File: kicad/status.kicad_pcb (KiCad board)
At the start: 4 copper layers, 84.1 x 61.7 mm, 49 parts, among them J1 Bus_PCI_Express_x1, J2 PPTC041LGBN-RC, J3 Conn_01x04, J4 503398-1892, J6 USB_C_Receptacle_USB2.0_16P, J7 Conn_01x02, U1 MCP25625T-E/ML, U2 RP2040, U4 W25Q128JVP, X1 ABM8-272-T3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

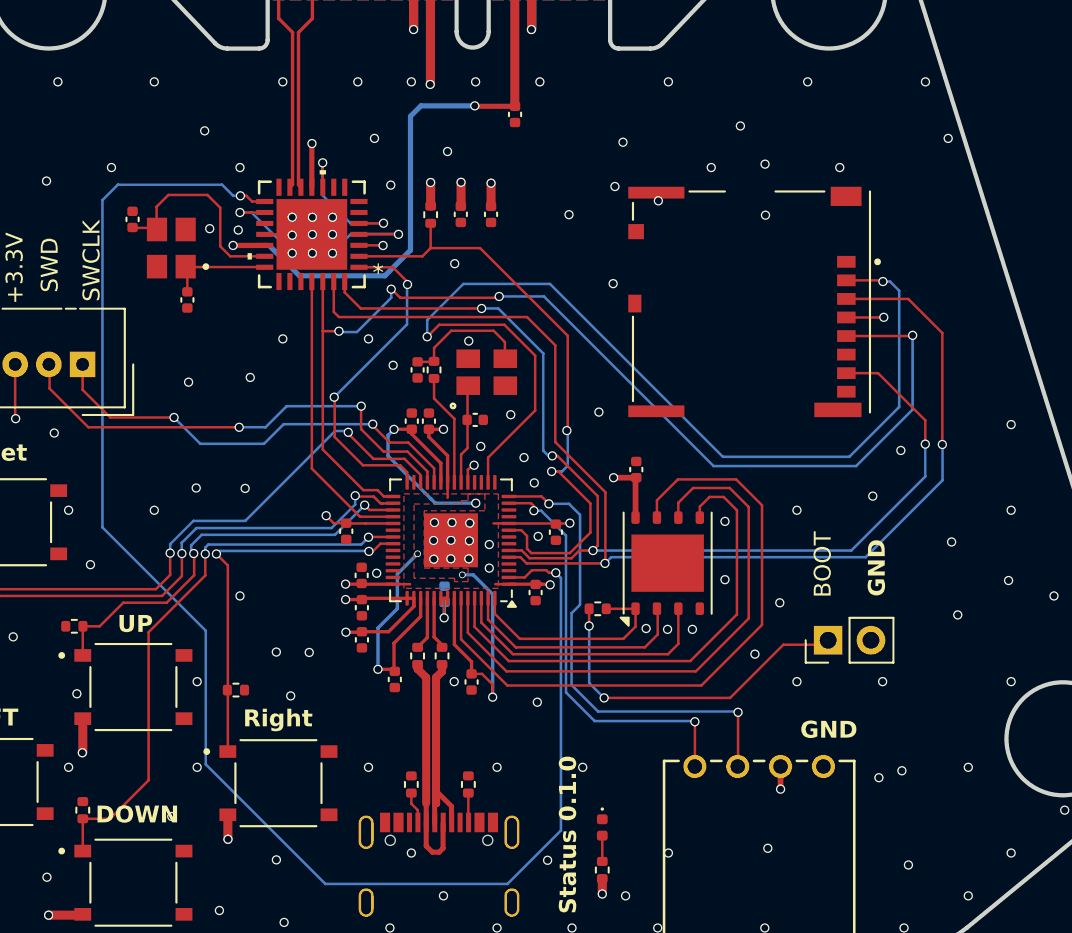
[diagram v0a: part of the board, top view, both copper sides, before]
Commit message: Pcb layout updated
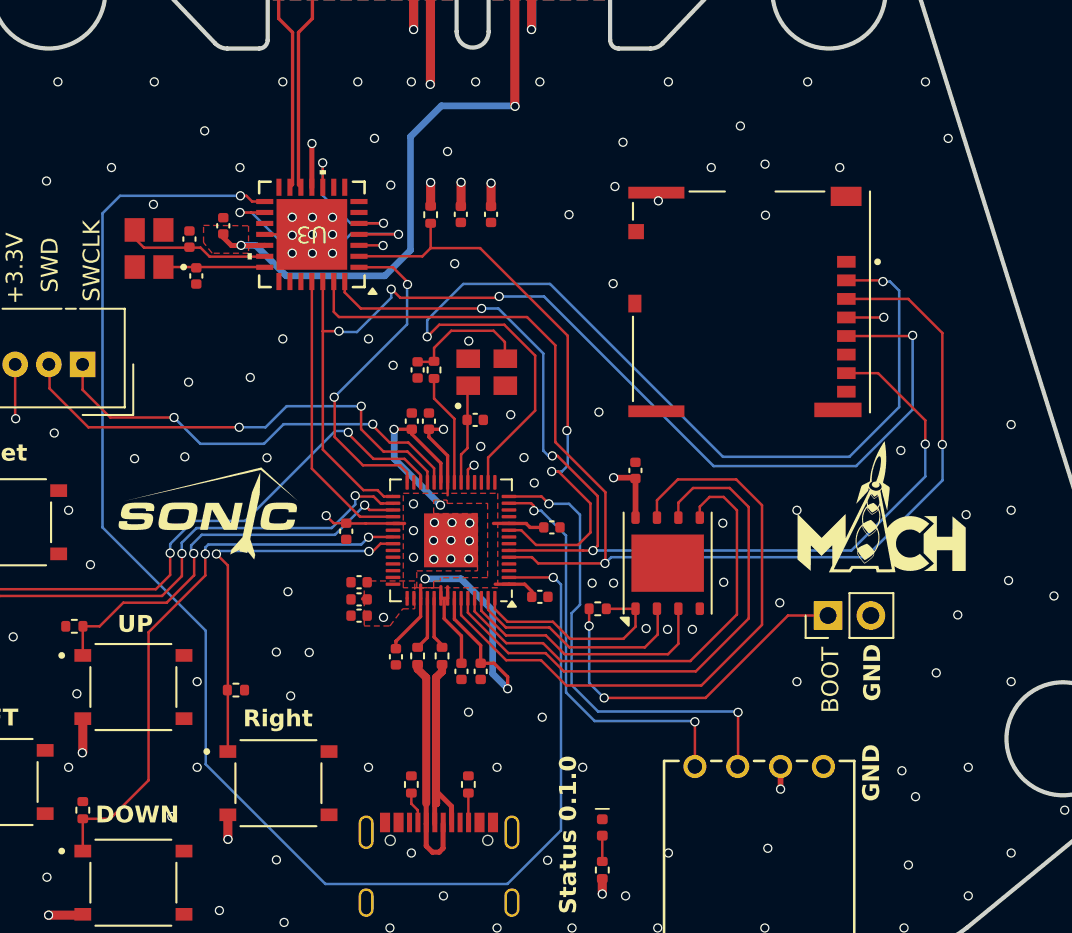
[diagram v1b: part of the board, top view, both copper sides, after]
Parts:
- removed U1: MCP25625T-E/ML, challenge_template:QFN28_6X6MC_MCH
- added G***: LOGO, LOGO, F.Cu at (172.7, 97.3)
- added U3: MCP25625T-E/ML, challenge_template:QFN28_6X6MC_MCH, F.Cu at (138.9, 80.2)
- C11: moved to F.Cu
- moved C3 18.5 mm to (133.6, 79.7), turned to -90 degrees
- moved C11 4.68 mm to (147.8, 106.1), turned to 90 degrees
- moved C6 3.57 mm to (131.6, 80.4)
- moved C22 1.52 mm to (132.0, 82.6)
- moved J7 1.47 mm to (169.5, 102.8)
- moved C13 1.44 mm to (141.7, 102.8), turned to 0 degrees
- moved C9 1.34 mm to (143.9, 105.2)
- moved Y1 1.32 mm to (129.2, 81.0)
- moved C8 0.83 mm to (148.9, 106.1)
- moved C12 0.52 mm to (141.7, 101.8), turned to 0 degrees
- moved C14 0.43 mm to (141.7, 100.8), turned to 0 degrees
- moved C15 0.37 mm to (153.1, 97.5), turned to 180 degrees
- moved C7 0.36 mm to (152.4, 101.7), turned to 180 degrees
- moved C17 0.07 mm to (158.1, 94.2)
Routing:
- net +3.3V: track 81.5 -> 70.6 mm, vias 27 -> 23
- net +1V1: track 42.6 -> 32.1 mm, vias 6 -> 4
- net /OSC2: track 12.2 -> 8.66 mm
- net /STBY: track 90.3 -> 88.7 mm
- net +5V: track 48.5 -> 49.7 mm
- net /RESET: track 36.2 -> 35.4 mm
- net /QSPI_SD3: track 38.4 -> 37.6 mm
- net /QSPI_CLK: track 33.4 -> 32.7 mm
- net /~{USB_BOOT_S}: track 20.3 -> 21.0 mm
- net /QSPI_SD0: track 28.8 -> 28.3 mm
- net GND: track 4.24 -> 4.44 mm, vias 144 -> 141
- added copper zone on F.Cu, net +5V

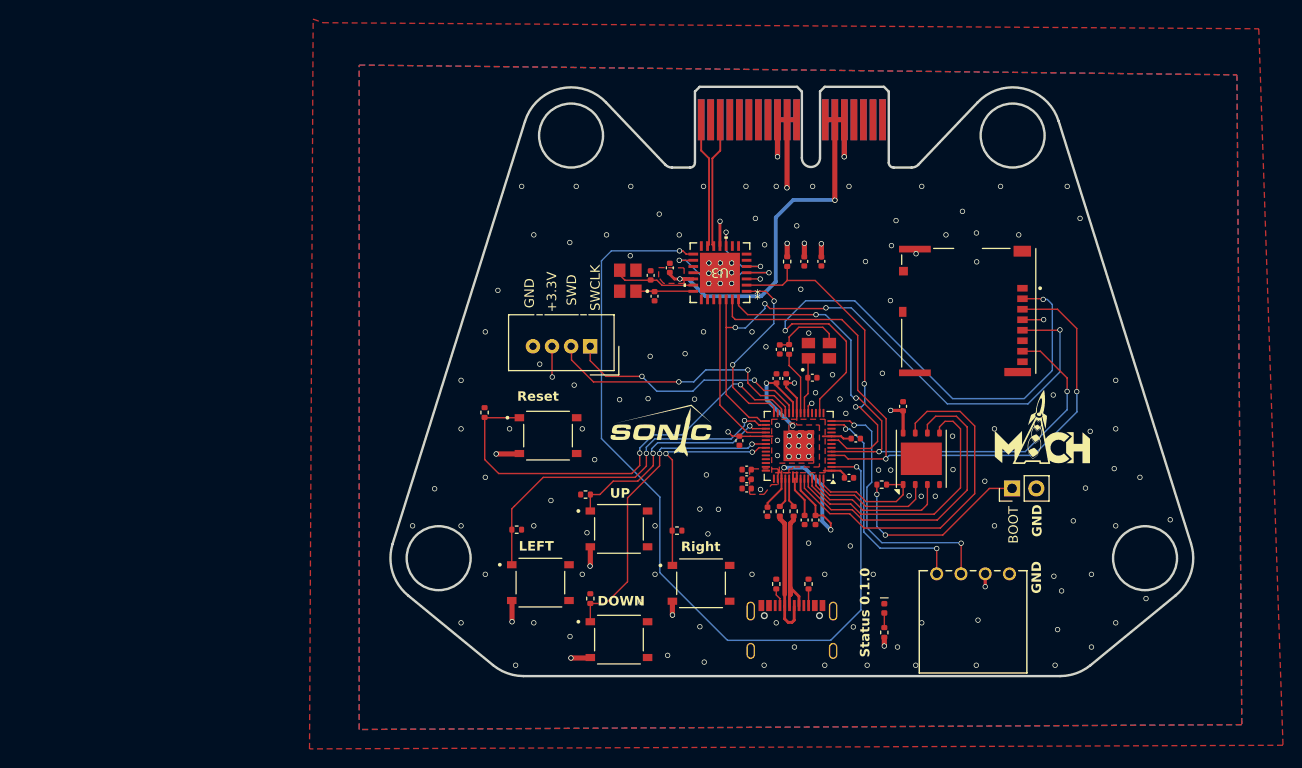
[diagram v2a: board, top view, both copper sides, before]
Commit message: General Updates
Moved CAN transmitter to separate SPI line.
Updated rp2040 clock.
Fixed debug pins.
Updated nets.
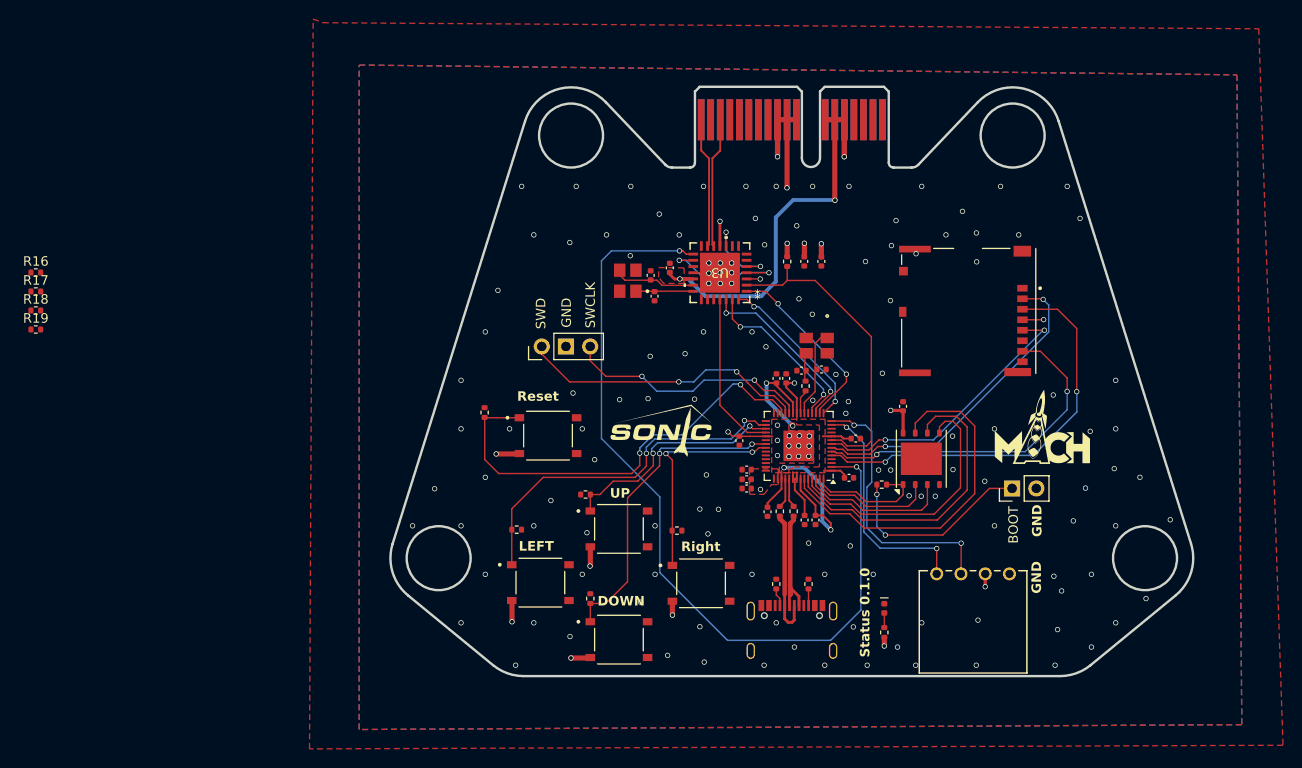
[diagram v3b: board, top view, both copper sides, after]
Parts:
- added R16: 10K, Resistor_SMD:R_0402_1005Metric, F.Cu at (67.2, 80.1)
- added R17: 10K, Resistor_SMD:R_0402_1005Metric, F.Cu at (67.2, 82.1)
- added R18: 10K, Resistor_SMD:R_0402_1005Metric, F.Cu at (67.2, 84.1)
- added R19: 10K, Resistor_SMD:R_0402_1005Metric, F.Cu at (67.2, 86.1)
- J3: value Conn_01x04 -> Conn_01x03; footprint Connector:NS-Tech_Grove_1x04_P2mm_Vertical -> Connector_PinHeader_2.54mm:PinHeader_1x03_P2.54mm_Vertical
- X1: footprint challenge_template:ABM8-272-T3_ABR -> 4in-kicad-library:ABM8-272-T3_ABR
- moved J3 5.08 mm to (120.2, 87.9), turned to 90 degrees
- moved R3 4.20 mm to (147.8, 92.0)
- moved C18 3.18 mm to (147.4, 90.4), turned to 180 degrees
- moved C23 1.29 mm to (149.5, 90.3)
- moved X1 0.58 mm to (149.0, 87.8), turned to -90 degrees
- renumbered J1 to J5
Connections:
- net /X_IN renamed /XIN
- net /X_OUT renamed /XOUT
- J3 pad 1: /SWCLK -> /SWD
- J3 pad 2: /SWD -> GND
- J3 pad 3: +3.3V -> /SWCLK
- U2 pad 15: unconnected-(U2-GPIO12-Pad15) -> /MISO_CAN
- U2 pad 16: /CS_SD -> /CS_CAN
- U2 pad 17: unconnected-(U2-GPIO14-Pad17) -> /SCK_CAN
- U2 pad 18: unconnected-(U2-GPIO15-Pad18) -> /MOSI_CAN
- U2 pad 28: /CS -> unconnected-(U2-GPIO17-Pad28)
- U2 pad 29: /SCK -> unconnected-(U2-GPIO18-Pad29)
- U2 pad 7: unconnected-(U2-GPIO5-Pad7) -> /CS_SD
- U2 pad 8: unconnected-(U2-GPIO6-Pad8) -> /SCK
- U3 pad 1: /CS -> /CS_CAN
- U3 pad 26: /SCK -> /SCK_CAN
- U3 pad 27: /MOSI -> /MOSI_CAN
- U3 pad 28: /MISO -> /MISO_CAN
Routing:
- net /SCK: track 65.8 -> 30.1 mm, vias 4 -> 2
- net /MOSI: track 73.1 -> 43.5 mm
- net /CS_SD: track 61.8 -> 34.2 mm
- net /MISO: track 63.1 -> 36.3 mm, vias 4 -> 2
- net /CS: track 20.0 -> 0.00 mm, vias 2 -> 0
- net /CS_CAN: track 0.00 -> 19.4 mm, vias 0 -> 2
- net /SCK_CAN: track 0.00 -> 18.9 mm, vias 0 -> 2
- net /MOSI_CAN: track 0.00 -> 17.6 mm, vias 0 -> 2
- net /MISO_CAN: track 0.00 -> 17.4 mm, vias 0 -> 2
- net Net-(C18-Pad1): track 7.30 -> 3.00 mm
- net /XOUT: track 6.64 -> 2.41 mm
- net /XIN: track 5.91 -> 9.24 mm
- net +3.3V: track 70.6 -> 67.4 mm, vias 23 -> 22
- net /RESET: track 35.4 -> 32.8 mm, vias 2 -> 0
- net /SWD: track 28.7 -> 30.3 mm
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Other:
- board text removed: "+3.3V"

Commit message: General update schematic and PCB
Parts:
- J3: footprint Connector_PinHeader_2.54mm:PinHeader_1x03_P2.54mm_Vertical -> challenge_template:PinHeader_1x03_P2.54mm_Vertical
- X1: footprint 4in-kicad-library:ABM8-272-T3_ABR -> challenge_template:ABM8-272-T3_ABR
- moved R18 107.0 mm to (174.0, 90.0), turned to 90 degrees
- moved R17 106.9 mm to (174.0, 87.8), turned to -90 degrees
- moved R16 106.9 mm to (174.0, 84.5), turned to 90 degrees
- moved R19 106.9 mm to (174.0, 82.3), turned to 90 degrees
- moved C5 9.06 mm to (139.4, 75.5), turned to 0 degrees
- moved C4 5.41 mm to (144.2, 80.2), turned to 90 degrees
- moved R15 2.74 mm to (114.8, 97.5), turned to 0 degrees
- moved R7 1.92 mm to (117.6, 109.0)
- moved R9 1.82 mm to (134.4, 109.0)
- moved R8 1.07 mm to (125.8, 115.2), turned to 0 degrees
- moved C11 0.95 mm to (147.8, 105.1)
- moved R13 0.78 mm to (145.8, 79.8), turned to 0 degrees
- moved C7 0.15 mm to (152.4, 101.8)
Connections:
- J4 pad 1: unconnected-(J4-DAT2-Pad1) -> Net-(J4-DAT2)
- J4 pad 8: unconnected-(J4-DAT1-Pad8) -> Net-(J4-DAT1)
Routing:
- net +3.3V: track 67.4 -> 58.3 mm, vias 22 -> 21
- net +1V1: track 32.1 -> 28.1 mm
- net /TX: track 14.2 -> 17.7 mm
- net Net-(J4-DAT2): track 0.00 -> 3.47 mm
- net Net-(J4-DAT1): track 0.00 -> 3.43 mm
- net /Push_Down: track 33.3 -> 31.4 mm, vias 2 -> 0
- net /Push_Right: track 22.7 -> 20.9 mm, vias 2 -> 0
- net /MISO: track 36.3 -> 37.5 mm
- net /CS_SD: track 34.2 -> 35.1 mm
- net /SCL: track 28.9 -> 28.2 mm
- net /SCK: track 30.1 -> 30.8 mm
- net /SDA: track 24.5 -> 23.9 mm
- net /RX: track 9.12 -> 8.59 mm, vias 2 -> 0
- net GND: vias 139 -> 140

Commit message: PCB Layout Update
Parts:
- removed J7: Conn_01x02, Connector_PinHeader_2.54mm:PinHeader_1x02_P2.54mm_Vertical
- removed R15, R7, R8: 10K, Resistor_SMD:R_0402_1005Metric
- added R20: 10K, Resistor_SMD:R_0402_1005Metric, F.Cu at (125.8, 114.9)
- added R21: 10K, Resistor_SMD:R_0402_1005Metric, F.Cu at (125.9, 103.3)
- added R22: 10K, Resistor_SMD:R_0402_1005Metric, F.Cu at (117.6, 108.9)
- added R24: 1k, Resistor_SMD:R_0402_1005Metric, F.Cu at (119.0, 116.8)
- added R25: 1k, Resistor_SMD:R_0402_1005Metric, F.Cu at (126.9, 111.0)
- added R26: 1k, Resistor_SMD:R_0402_1005Metric, F.Cu at (123.2, 120.5)
- added S12: TS-1187A-B-A-B, Nicolas Library:SW_TS-1187A-B-A-B, F.Cu at (172.2, 103.8)
- moved R10 10.8 mm to (134.4, 108.3)
- moved C13 10.8 mm to (152.4, 101.8), turned to 180 degrees
- moved C7 10.7 mm to (141.7, 102.8), turned to 0 degrees
- moved R9 7.82 mm to (135.4, 116.8)
- moved G*** 0.73 mm to (171.9, 97.5)
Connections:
- R10 pad 1: /Push_Up -> GND
- R10 pad 2: GND -> /Push_Right
- R9 pad 1: /Push_Right -> Net-(R9-Pad1)
- R9 pad 2: GND -> +3.3V
- S10 pad C: +3.3V -> Net-(R9-Pad1)
- S11 pad A: /RUN -> GND
- S11 pad C: +3.3V -> /RUN
- S7 pad C: +3.3V -> Net-(R24-Pad1)
- S8 pad C: +3.3V -> Net-(R25-Pad1)
- S9 pad C: +3.3V -> Net-(R26-Pad1)
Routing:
- net /RUN: track 45.9 -> 35.8 mm
- net +3.3V: track 58.3 -> 52.4 mm, vias 21 -> 20
- net Net-(R24-Pad1): track 0.00 -> 3.15 mm
- net Net-(R25-Pad1): track 0.00 -> 2.92 mm
- net Net-(R9-Pad1): track 0.00 -> 2.90 mm
- net Net-(R26-Pad1): track 0.00 -> 1.76 mm
- net /~{USB_BOOT_S}: track 21.0 -> 19.4 mm
- net /STBY: track 88.7 -> 87.3 mm
- net /Push_Down: track 31.4 -> 32.7 mm
- net /Push_Right: track 20.9 -> 21.7 mm
- net /Push_Left: track 37.7 -> 37.0 mm
- added copper zone on In2.Cu, net +3.3V
- added copper zone on In1.Cu, net GND
- removed copper zone on In1.Cu, net +3.3V
- removed copper zone on In2.Cu, net GND
